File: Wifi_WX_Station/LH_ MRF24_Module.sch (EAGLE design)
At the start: 7 parts, among them M1 MRF24WB0MA

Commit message: added all the small boards, renamed Wifi module as RH and LH version
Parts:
- C1, C2: value (none) -> 0.1uF
- C3: value (none) -> 4.7uF
- JP1: value M05X2RAF -> M05X2; device wifi_WX:M05X2RAF -> wifi_WX:M05X2
- R1: value 4.7k -> 4.7K
- R2: value 10k -> 10K
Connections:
- net GND: now also M1.GND@2, M1.NC@3; no longer M1.GND@12, M1.JTAGRST_
- net RESET_: now also M1.NC@2; no longer M1.RESET_
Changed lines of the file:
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@@
 <part name="+3V6" library="supply1" deviceset="+3V3" device=""/>
 <part name="M1" library="1AA_Stofer" deviceset="MR24WB0MA" device="" value="MRF24WB0MA"/>
-<part name="R2" library="rcl" deviceset="R-US_" device="R0603" value="10k"/>
+<part name="R2" library="rcl" deviceset="R-US_" device="R0603" value="10K"/>
 <part name="SUPPLY10" library="supply2" deviceset="GND" device=""/>
 <part name="SUPPLY11" library="supply2" deviceset="GND" device=""/>
@@
 <part name="+3V18" library="supply1" deviceset="+3V3" device=""/>
 <part name="SUPPLY28" library="supply2" deviceset="GND" device=""/>
-<part name="C1" library="rcl" deviceset="C-US" device="C0805"/>
-<part name="C2" library="rcl" deviceset="C-US" device="C0805"/>
-<part name="R1" library="rcl" deviceset="R-US_" device="R0603" value="4.7k"/>
-<part name="C3" library="rcl" deviceset="CPOL-US" device="R/2012-12R"/>
-<part name="JP1" library="wifi_WX" deviceset="M05X2" device="RAF"/>
+<part name="C1" library="rcl" deviceset="C-US" device="C0805" value="0.1uF"/>
+<part name="C2" library="rcl" deviceset="C-US" device="C0805" value="0.1uF"/>
+<part name="R1" library="rcl" deviceset="R-US_" device="R0603" value="4.7K"/>
+<part name="C3" library="rcl" deviceset="CPOL-US" device="R/2012-12R" value="4.7uF"/>
+<part name="JP1" library="wifi_WX" deviceset="M05X2" device="" value="M05X2"/>
 </parts>
 <sheets>
@@
 </segment>
 <segment>
-<pinref part="M1" gate="G$1" pin="GND@12"/>
-<pinref part="M1" gate="G$1" pin="JTAGRST_"/>
+<pinref part="M1" gate="G$1" pin="NC@3"/>
+<pinref part="M1" gate="G$1" pin="GND@2"/>
 <wire x1="10.16" y1="30.48" x2="12.7" y2="30.48" width="0.1524" layer="91"/>
 <wire x1="12.7" y1="33.02" x2="10.16" y2="33.02" width="0.1524" layer="91"/>
@@
 <net name="RESET_" class="0">
 <segment>
-<pinref part="M1" gate="G$1" pin="RESET_"/>
+<pinref part="M1" gate="G$1" pin="NC@2"/>
 <wire x1="12.7" y1="38.1" x2="2.54" y2="38.1" width="0.1524" layer="91"/>
 <wire x1="2.54" y1="38.1" x2="2.54" y2="71.12" width="0.1524" layer="91"/>

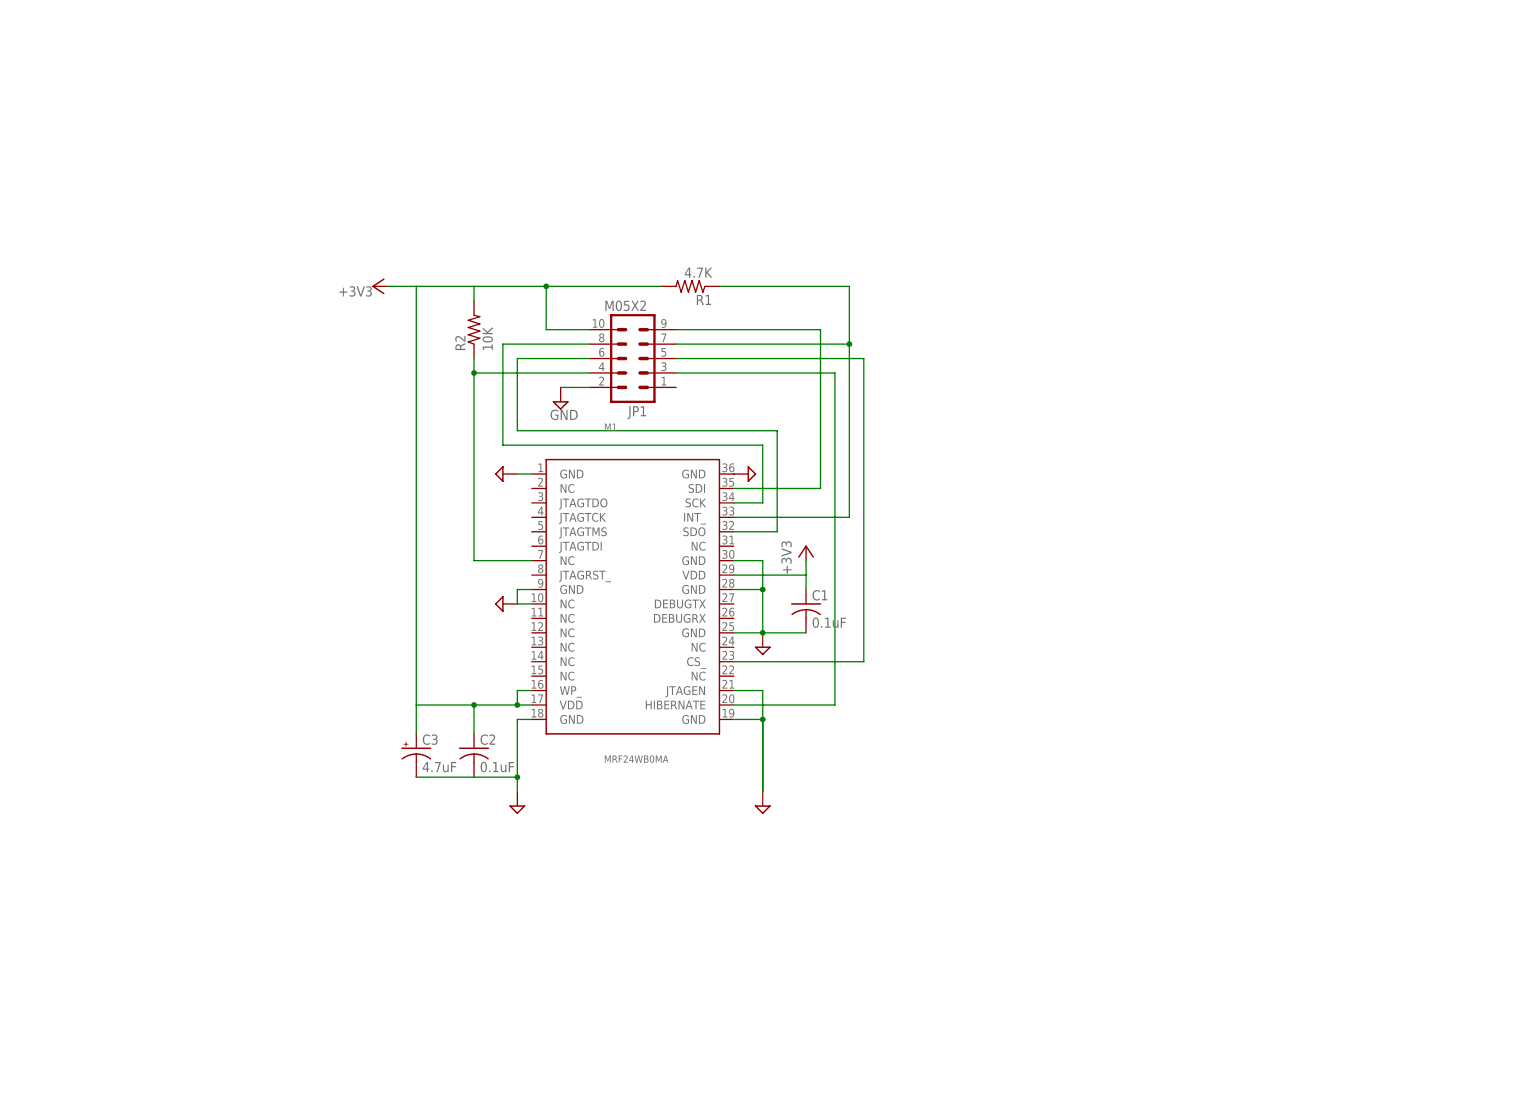
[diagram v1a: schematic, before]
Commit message: added SILabs Hygrometer board Added frames to the schematics
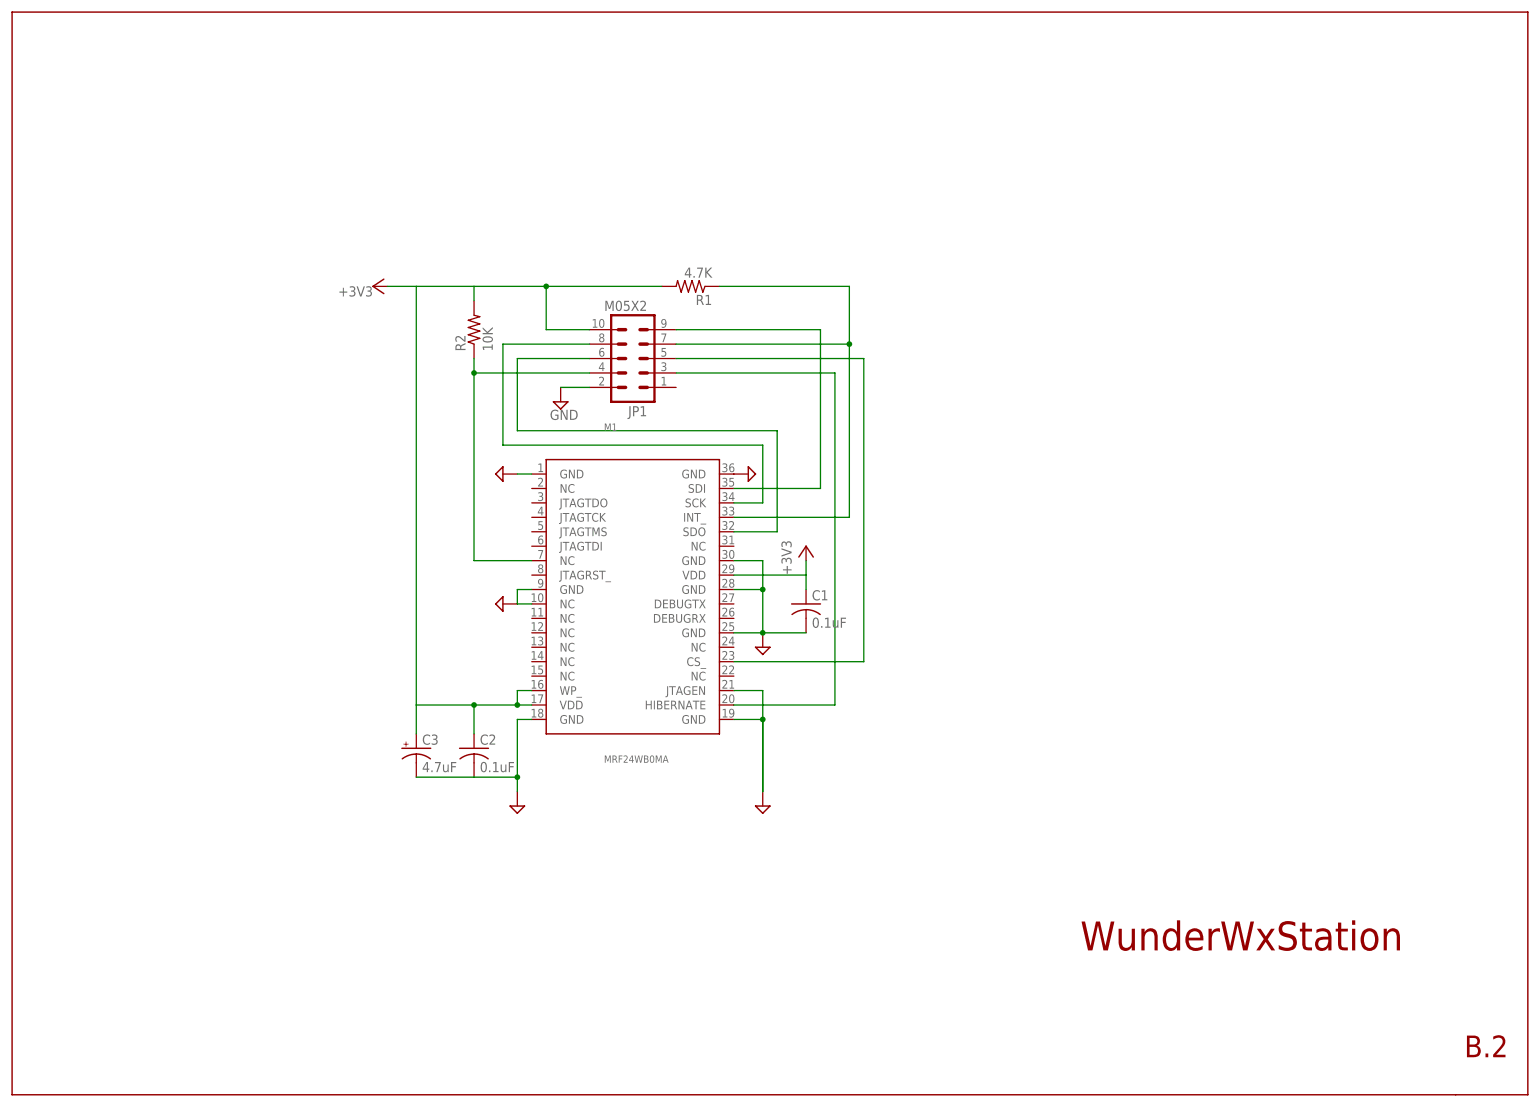
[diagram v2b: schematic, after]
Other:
- note added: "B.2"
- note added: "WunderWxStation"
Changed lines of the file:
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@@
 <part name="C3" library="rcl" deviceset="CPOL-US" device="R/2012-12R" value="4.7uF"/>
 <part name="JP1" library="wifi_WX" deviceset="M05X2" device="" value="M05X2"/>
+<part name="U$1" library="1AA_Stofer" deviceset="8.5X11" device=""/>
 </parts>
 <sheets>
 <sheet>
 <plain>
+<text x="109.22" y="-30.48" size="5.08" layer="94" ratio="20">WunderWxStation</text>
+<text x="176.784" y="-49.276" size="3.81" layer="94" ratio="20">B.2</text>
 </plain>
 <instances>
@@
 <instance part="C3" gate="G$1" x="-7.62" y="5.08"/>
 <instance part="JP1" gate="G$1" x="30.48" y="73.66" rot="R180"/>
+<instance part="U$1" gate="G$1" x="-78.74" y="-55.88"/>
+<instance part="U$1" gate="G$2" x="86.36" y="-55.88"/>
 </instances>
 <busses>
